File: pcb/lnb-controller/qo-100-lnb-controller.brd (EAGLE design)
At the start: 70 x 100 mm, 172 parts, among them CON1 2EDG-2P, U1 EFM32PG1B200F256GM32, U10 ADP7142AUJZ-3.3, U2 IQXT-210-3, U3 DSB321SDA, U4 SI5351C-B-GM1, U5 LT8650S-1, U6 AD5272-100, U7 AD5272-100, U8 MIC23155, U9 LT8636

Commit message: Work on LNB Controller
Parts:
- removed C83: 10uF, Capacitor:CAP1206
- removed JP1: PINHD-1X3, Pin Header:1X03
- removed L21: 4.7uH, Inductor:IND2520
- removed R42: 510 Ohms, Resistor:RES0603
- added C26: 100nF, Capacitor:CAP0603
- added CON2: 2EDG-2P-5MM, Generic Connector:2EDG-2P-5MM
- C11: value 100nF -> 330pF
- C13, C21: value 330pF -> 100pF
- C17: value 100pF -> 1nF
- C19: value 1nF -> 330pF
- C23: value 100pF -> 68pF
- C25: value 68pF -> 100nF
- C27: value 100nF -> 33nF
- C28: value 100nF -> 15pF
- C3: value 4.7uF -> 100nF
- C30, C75: value 100nF -> 10pF
- C31: value 15pF -> 100nF
- C33: value 10pF -> 100nF
- C34, C54, C63, C80: value 100nF -> 1uF
- C35, C71: value 1uF -> 10nF
- C37, C72: value 10nF -> 470pF
- C38, C73: value 470pF -> 100nF
- C40: value 100nF -> 4.7uF
- C41: value 4.7uF -> 4.7pF
- C43: value 4.7pF -> 1uF
- C44, C55: value 1uF -> 22uF; device Capacitor:CAP0603 -> Capacitor:CAP1206
- C48, C59: value 22uF -> 100nF; device Capacitor:CAP1206 -> Capacitor:CAP0603
- C51, C61: value 100nF -> 10uF
- C52, C62: value 10uF -> 100nF
- C64: value 1uF -> 4.7uF
- C66: value 4.7uF -> 470pF
- C68: value 470pF -> 1uF
- C7: value 100nF -> 100pF
- C76: value 10pF -> 470pF
- C77: value 470pF -> 100uF; device Capacitor:CAP0603 -> Capacitor:CAP1206
- C79: value 100uF -> 100nF; device Capacitor:CAP1206 -> Capacitor:CAP0603
- C81: value 1uF -> 10uF
- C82: device Capacitor:CAP0603 -> Capacitor:CAP1206
- C9: value 100pF -> 100nF
- CON1: value 2EDG-2P -> 3P-SH-SIDE; device Generic Connector:2EDG-2P -> JST:SH-03-SIDE
- L1: value 4.7uH -> 470nH
- L10, L12: value 43nH -> 330nH
- L11: value 330nH -> 43nH
- L13: value 330nH -> 470nH
- L14, L16, L7: value 470nH -> 120nH
- L15: value 120nH -> 470nH
- L17: value 120nH -> 4.7uH; device Inductor:IND0603 -> Inductor:IND0404
- L19: value 4.7uH -> 2.2uH; device Inductor:IND0404 -> Inductor:IND2520
- L20: value 2.2uH -> 4.7uH
- L9: value 120nH -> 43nH
- R10: value 10K Ohms -> 86.6 Ohms
- R11: value 8.4K Ohms -> 100K Ohms
- R12, R31: value 100K Ohms -> 10K Ohms
- R13: value 10K Ohms -> 0 Ohms
- R16: value 0 Ohms -> 100K Ohms
- R18: value 100K Ohms -> 15K Ohms
- R19: value 15K Ohms -> 100K Ohms
- R21: value 100K Ohms -> 1K Ohms
- R22: value 1K Ohms -> 1M Ohms
- R23, R26: value 1M Ohms -> DNP
- R24, R27: value DNP -> 40.2K Ohms
- R25: value 40.2K Ohms -> 1M Ohms
- R28: value 40.2K Ohms -> 2.5K Ohms
- R30: value 2.5K Ohms -> 100K Ohms
- R32: value 10K Ohms -> 90.9K Ohms
- R33, R38: value 90.9K Ohms -> 12K Ohms
- R34: value 12K Ohms -> 41.2K Ohms
- R35: value 41.2K Ohms -> 309K Ohms
- R36: value 309K Ohms -> 71.5K Ohms
- R37: value 71.5K Ohms -> 90.9K Ohms
- R39: value 12K Ohms -> 1M Ohms
- R4: value 10K Ohms -> 100 Ohms
- R40: value 1M Ohms -> 226K Ohms
- R41: value 226K Ohms -> 510 Ohms
- R5: value 330 Ohms -> 100 Ohms
- R6: value 43.2 Ohms -> 330 Ohms
- R8: value 86.6 Ohms -> 43.2 Ohms
- U1: value EFM32PG1B200F256GM32 -> EFM32PG1B100F256GM32
- U2: value IQXT-210-3 -> TX-8010-EAW-1070-25M0000000; device Crystal:IQXT-210-23 -> Microchip:TCXO-5032
- U4: value SI5351C-B-GM1 -> SI5351C-B-GM; device Silicon Labs:QFN16 -> Silicon Labs:QFN20
- moved R10 99.8 mm to (32.9, 80.8), turned to 270 degrees
- moved U2 88.5 mm to (46.1, 34.5), turned to 0 degrees
- moved C27 87.5 mm to (47.5, 37.7)
- moved C31 79.8 mm to (56.2, 29.7), turned to 270 degrees
- moved R11 73.8 mm to (57.0, 58.0), turned to 270 degrees
- moved C11 62.1 mm to (46.0, 20.9)
- moved L8 61.8 mm to (46.0, 80.9)
- moved C16 61.6 mm to (49.0, 80.8), turned to 90 degrees
- moved R9 61.6 mm to (32.9, 19.2), turned to 90 degrees
- moved L5 61.3 mm to (42.5, 20.8)
- moved R8 60.9 mm to (30.4, 80.0), turned to 180 degrees
- moved L7 60.2 mm to (46.0, 19.1), turned to 0 degrees
- moved C10 60.0 mm to (26.8, 80.0)
- moved C24 60.0 mm to (56.2, 80.0)
- moved R7 60.0 mm to (30.4, 20.0)
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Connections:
- removed net 1V8: C3.1, L1.1, U1.28
- removed net LNB_BIAS_SEL: C5.1, JP1.2, R4.2, U1.11
- removed net N$27 (its old number): C9.1, L3.2, L5.1
- removed net N$29 (its old number): C15.1, L7.2
- removed net REF_XO_VC: R10.1, R11.2, U2.1
- new net N$13: C7.1, L1.2, L3.1
- new net N$14: C13.1, L5.2
- new net N$38: CON1.1, R4.1
- new net N$4: CON1.2, R5.1
- new net UART_RX: R4.2, U1.4
- new net UART_TX: R5.2, U1.5
- net !REF_SYNTH_OE: now also R11.1, U1.32, U4.7; no longer R12.1, U1.10, U4.3
- net !RESET: now also U1.9; no longer U1.8
- net 3V3: now also C3.1, C51.1, C53.1, C61.1, C73.1, C77.1, L19.2, R11.2, R19.2, R35.2, U1.25, U1.6; no longer C52.1, C54.1, C63.1, C74.1, C78.1, JP1.1, L20.2, R12.2, R21.2, R36.2, U1.30, U1.5
- net 3V3_FB: now also R35.1, R36.2; no longer R36.1, R37.2
- net 3V3_REF_CLEAN: now also C25.1, C26.1, C31.1, C33.1, C81.1, U2.8, U2.9, U4.10, U4.18, U4.20; no longer C27.1, C28.1, C30.1, C34.1, C82.1, R10.2, U2.4, U4.16, U4.8, U4.9
- net 3V3_SOFTSTART: now also C67.1; no longer C68.1
- net 3V3_SW: now also L19.1; no longer L20.1
- net 5V0: now also C65.1, C75.1, C78.1, L20.2, R39.2, R41.2; no longer C66.1, C76.1, C81.1, L21.2, R40.2, R42.2
- net 5V0_BST: now also C74.2; no longer C75.2
- net 5V0_FB: now also C75.2, R39.1, R40.2; no longer C76.2, R40.1, R41.2
- net 5V0_INTVCC: now also C70.1; no longer C71.1
- net 5V0_RT: now also R34.2; no longer R35.2
- net 5V0_SS: now also C71.1; no longer C72.1
- net 5V0_SW: now also C74.1, L20.1; no longer C75.1, L21.1
- net BIAS_REG_TEMP: now also C37.1, R21.1; no longer C38.1, R22.1
- net GND: now also C17.2, C25.2, C26.2, C33.2, C40.2, C43.2, C76.2, CON1.3, CON2.P$1, L10.1, L11.2, L12.1, L9.2, R10.1, R12.1, R16.1, R24.1, R27.1, R31.1, R33.1, R36.1, R38.1, R40.1, U2.10, U2.4, U2.5, U4.21; no longer C19.2, C32.2, C38.2, C41.2, C74.2, C83.2, C9.2, CON1.P$1, JP1.3, L10.2, L11.1, L12.2, L13.1, R11.1, R13.1, R19.1, R25.1, R28.1, R32.1, R35.1, R37.1, R39.1, R4.1, R41.1, R8.1, U1.25, U2.2, U4.15, U4.17
- net I2C_SCL: now also U1.31; no longer U1.32
- net I2C_SDA: now also U1.30; no longer U1.31
- net LED: now also R6.2, U1.29; no longer R5.2, U1.4
- net N$1: now also R15.2, U4.15; no longer R16.2, U4.12
- net N$10: now also C9.2, R7.2; no longer C10.2, R6.2
- net N$11: now also R28.1; no longer R29.1
- net N$12: now also C21.1, L13.2; no longer C22.1, L14.2
- net N$149: now also R41.1; no longer R42.1
- net N$15: now also C13.2, C17.1, L13.1, L9.1; no longer C14.2, C18.1, L10.1, L14.1
- net N$16: now also C19.2, C23.1, L14.2; no longer C20.2, C24.1, L15.2
- net N$17: now also C11.1, L5.1, L7.1, R7.1, R9.2; no longer C12.1, L6.1, L8.1, R6.1, R8.2
- net N$18: now also C11.2, C15.1, C19.1, L14.1, L7.2; no longer C12.2, C16.1, C20.1, L15.1, L8.2
- net N$19: now also CON2.P$2; no longer CON1.P$2
- net N$2: now also R14.2, U4.17; no longer R15.2, U4.13
- net N$20: now also C23.2; no longer C24.2
- net N$21: now also C27.1, U2.7; no longer L1.2, U1.26
- net N$22: now also C15.2, L10.2; no longer C16.2, L11.2
- net N$23: now also R29.1; no longer R30.1
- net N$24: now also C10.1, L4.2; no longer C11.1, L5.2
- net N$25: now also R6.1; no longer R5.1
- net N$26: now also C10.2, R8.2; no longer C11.2, R7.2
- net N$28: now also C22.1, L15.2; no longer C23.1, L16.2
- net N$3: now also R18.2; no longer R19.2
- net N$30: now also C14.2, C18.1, L11.1, L15.1; no longer C15.2, C19.1, L12.1, L16.1
- net N$31: now also C12.1, L6.1, L8.1, R10.2, R8.1; no longer C13.1, L7.1, L9.1, R7.1, R9.2
- net N$32: now also C12.2, C16.1, C20.1, L16.1, L8.2; no longer C13.2, C17.1, C21.1, L17.1, L9.2
- net N$33: now also C24.2; no longer C25.2
- net N$34: now also C16.2, L12.2; no longer C17.2, L13.2
- net N$35: now also C20.2, C24.1, L16.2; no longer C21.2, C25.1, L17.2
- net N$36: now also C32.2; no longer C33.2
- net N$37: now also C28.1, U2.6; no longer C31.1, U2.3
- net N$39: now also C54.1; no longer C55.1
- net N$40: now also C63.1; no longer C64.1
- net N$41: now also R15.1; no longer R16.1
- net N$5: now also R13.2, U4.12; no longer R14.2, U4.10
- net N$6: now also U1.26; no longer U1.29
- net N$7: now also C30.1, R12.2; no longer C33.1, R13.2
- net N$8: now also R21.2; no longer R22.2
- net N$9: now also C9.1, L3.2; no longer C10.1, L4.2
- net REF1: now also C21.2, R13.1; no longer C22.2, R14.1
- net REF2: now also C22.2, R14.1; no longer C23.2, R15.1
- net VBIAS1: now also C5.1, C55.1, C57.1, C59.1, L1.1, R28.2, R32.2; no longer C56.1, C58.1, C6.1, C60.1, L2.1, R29.2, R33.2
- net VBIAS1_BST: now also C38.2; no longer C39.2
- net VBIAS1_EN: now also R16.2; no longer R17.2
- net VBIAS1_FB: now also C41.2, R22.1, R23.2; no longer C42.2, R23.1, R24.2
- net VBIAS1_FB_DIV: now also R23.1, R24.2; no longer R24.1, R25.2
- net VBIAS1_PG: now also R19.1; no longer R20.1
- net VBIAS1_SS: now also C35.1; no longer C36.1
- net VBIAS1_SW: now also C38.1, L17.1; no longer C39.1, L18.1
- net VBIAS1_UNFUSED: now also C41.1, C44.1, C46.1, C48.1, C50.1, L17.2, R22.2; no longer C42.1, C45.1, C47.1, C49.1, C51.1, L18.2, R23.2
- net VBIAS1_VSENSE: now also C72.1, R32.1, R33.2; no longer C73.1, R33.1, R34.2
- net VBIAS2: now also C56.1, C58.1, C6.1, C60.1, L2.1, R29.2, R37.2; no longer C57.1, C59.1, C61.1, C7.1, L3.1, R30.2, R38.2
- net VBIAS2_BST: now also C39.2; no longer C40.2
- net VBIAS2_EN: now also R17.2; no longer R18.2
- net VBIAS2_FB: now also C42.2, R25.1, R26.2; no longer C43.2, R26.1, R27.2
- net VBIAS2_FB_DIV: now also R26.1, R27.2; no longer R27.1, R28.2
- net VBIAS2_PG: now also R20.1; no longer R21.1
- net VBIAS2_SS: now also C36.1; no longer C37.1
- net VBIAS2_SW: now also C39.1, L18.1; no longer C40.1, L19.1
- net VBIAS2_UNFUSED: now also C42.1, C45.1, C47.1, C49.1, C52.1, L18.2, R25.2; no longer C43.1, C46.1, C48.1, C50.1, C53.1, L19.2, R26.2
- net VBIAS2_VSENSE: now also C76.1, R37.1, R38.2; no longer C77.1, R38.1, R39.2
- net VBIAS_VCC: now also C34.1; no longer C35.1
- net VIN: now also C40.1, C43.1, C64.1, C68.1, C82.1, R30.2; no longer C41.1, C44.1, C65.1, C70.1, C83.1, R31.2
- net VIN_VSENSE: now also C66.1, R30.1, R31.2; no longer C67.1, R31.1, R32.2
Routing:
- net VBIAS1_VSENSE: track 6.55 -> 86.5 mm, vias 0 -> 2
- net VBIAS1_PG: track 15.7 -> 86.2 mm, vias 1 -> 2
- net VBIAS2_PG: track 12.9 -> 82.1 mm, vias 1 -> 2
- net VBIAS1_EN: track 7.73 -> 74.4 mm, vias 1 -> 2
- net VBIAS2_EN: track 6.87 -> 72.7 mm, vias 1 -> 2
- net BIAS_REG_TEMP: track 5.98 -> 64.4 mm, vias 0 -> 2
- net LNB_BIAS_SEL: track 43.2 -> 0.00 mm, vias 4 -> 0
- net UART_RX: track 0.00 -> 33.3 mm, vias 0 -> 4
- net UART_TX: track 0.00 -> 32.9 mm, vias 0 -> 4
- net VBIAS2_VSENSE: track 5.65 -> 25.6 mm, vias 0 -> 2
- net 3V3_REF_CLEAN: track 45.7 -> 61.9 mm, vias 7 -> 9
- net VIN_VSENSE: track 1.80 -> 10.5 mm
- net LED: track 11.6 -> 3.30 mm, vias 2 -> 0
- net 3V3: track 35.2 -> 40.5 mm
- net N$37: track 0.00 -> 5.05 mm
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
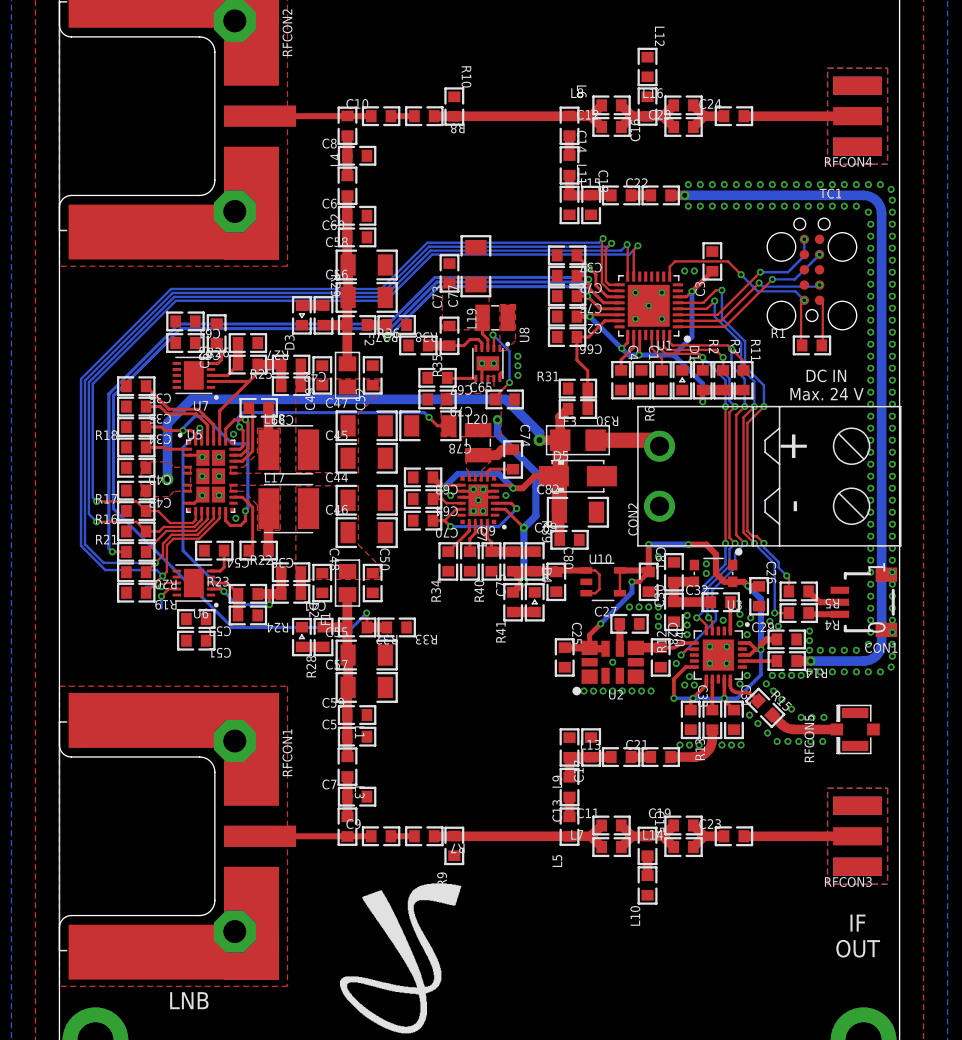
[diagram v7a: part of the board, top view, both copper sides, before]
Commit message: Nothing to do on LNB Controller
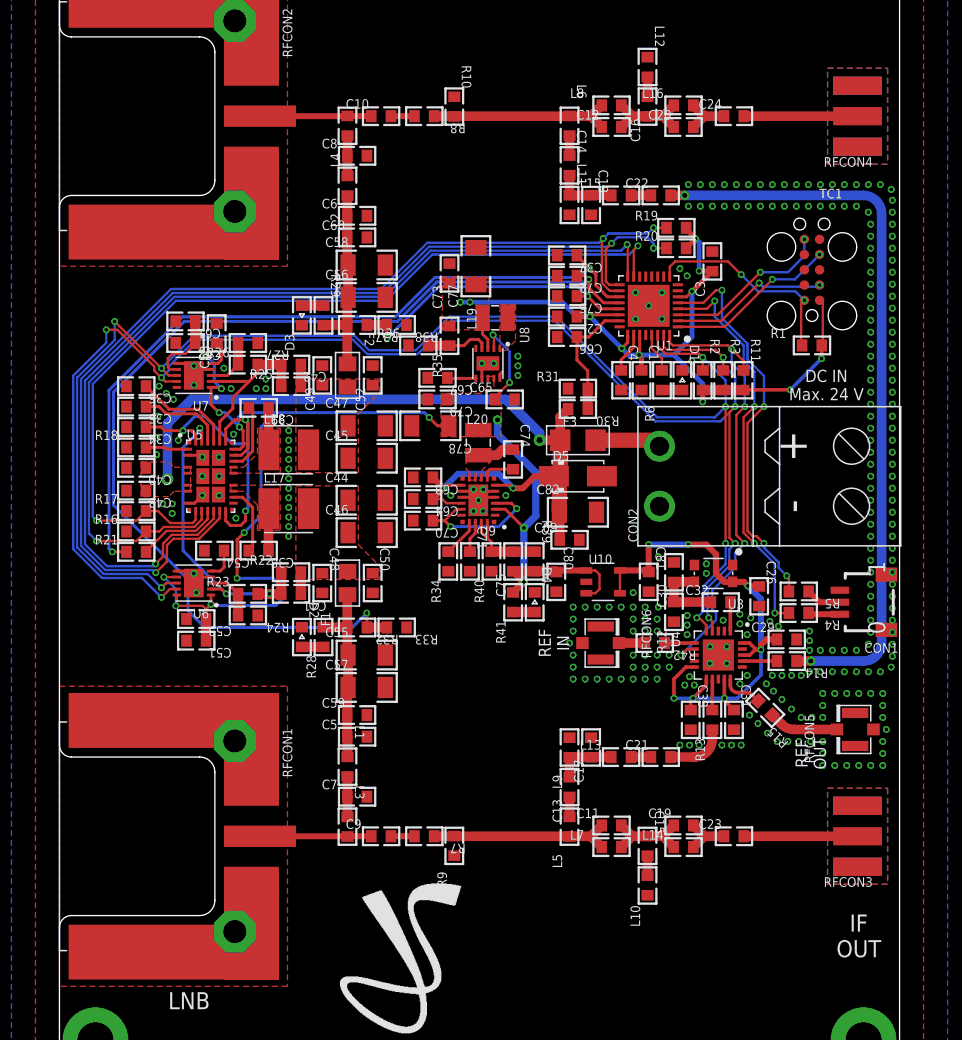
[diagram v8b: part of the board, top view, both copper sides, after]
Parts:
- removed C25: 100nF, Capacitor:CAP0603
- removed C27: 33nF, Capacitor:CAP0603
- removed C28: 15pF, Capacitor:CAP0603
- removed U2: TX-8010-EAW-1070-25M0000000, Microchip:TCXO-5032
- added R42: 0 Ohms, Resistor:RES0603
- added RFCON6: RFCON-U.FL, RF Connector:U.FL
- moved R19 54.3 mm to (51.4, 70.7), turned to 0 degrees
- moved R20 52.5 mm to (51.4, 69.0), turned to 0 degrees
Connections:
- net N$41 renamed EXT_REF_OUT
- removed net N$21: C27.1, U2.7
- new net EXT_REF_IN: R42.2, RFCON6.P$3
- net 3V3: no longer C51.1, C53.1, C61.1, C62.1, U6.1, U6.10, U6.7, U7.1, U7.7
- net 3V3_REF_CLEAN: no longer C25.1, U2.8, U2.9
- net 5V0: now also C51.1, C53.1, C61.1, C62.1, U6.1, U6.10, U6.7, U7.1, U7.7
- net GND: now also RFCON6.P$1, RFCON6.P$2; no longer C25.2, C27.2, C28.2, U2.10, U2.4, U2.5
- net N$37: now also R42.1; no longer C28.1, U2.6
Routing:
- net I2C_SCL: track 34.6 -> 124.9 mm, vias 5 -> 7
- net I2C_SDA: track 33.9 -> 121.8 mm, vias 5 -> 7
- net 5V0: track 59.9 -> 114.2 mm, vias 7 -> 15
- net 3V3: track 40.5 -> 68.2 mm, vias 5 -> 11
- net 3V3_REF_CLEAN: track 61.9 -> 49.7 mm, vias 9 -> 7
- net GND: track 11.2 -> 21.5 mm, vias 218 -> 289
- net VBIAS2_PG: track 82.1 -> 86.6 mm, vias 2 -> 3
- net VBIAS1_PG: track 86.2 -> 89.1 mm, vias 2 -> 3
- net N$37: track 5.05 -> 2.48 mm
- net EXT_REF_IN: track 0.00 -> 2.16 mm
- net N$21: track 2.08 -> 0.00 mm
- net N$25: track 0.00 -> 1.70 mm
- net N$34: track 0.00 -> 1.66 mm
- net VBIAS2_EN: track 72.7 -> 74.3 mm
- net VBIAS1_EN: track 74.4 -> 76.0 mm
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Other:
- board text added: "REF IN"
- board text added: "REF OUT"
